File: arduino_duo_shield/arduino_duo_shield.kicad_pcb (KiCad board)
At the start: 2 copper layers, 101.6 x 86.1 mm, 63 parts, among them J1 Spindle_Power, J2 Spindle_Control, J3 Motor_Control, J4 Limit_Switches, J5 Spindle_Relay_Power, J6 Spindle_Signal, J7 Power_In, K1 JQC-3F, P1 CONN_01X01, P10 Digital, P11 PWM, P12 PWM, P13 Communication, P14 CONN_01X01, P15 CONN_01X01, P16 CONN_01X01, P17 CONN_01X01, P2 CONN_01X01, P3 CONN_01X01, P4 CONN_01X01, P5 CONN_01X01, P6 CONN_01X01, P7 Power, P8 Analog, P9 Analog, Q1 2N7000, Q2 IRFZ44N, SW1 SW_Push, U1 4504, U2 4504, U3 PC817, U4 74HC14, U5 PC817, U6 74HC14

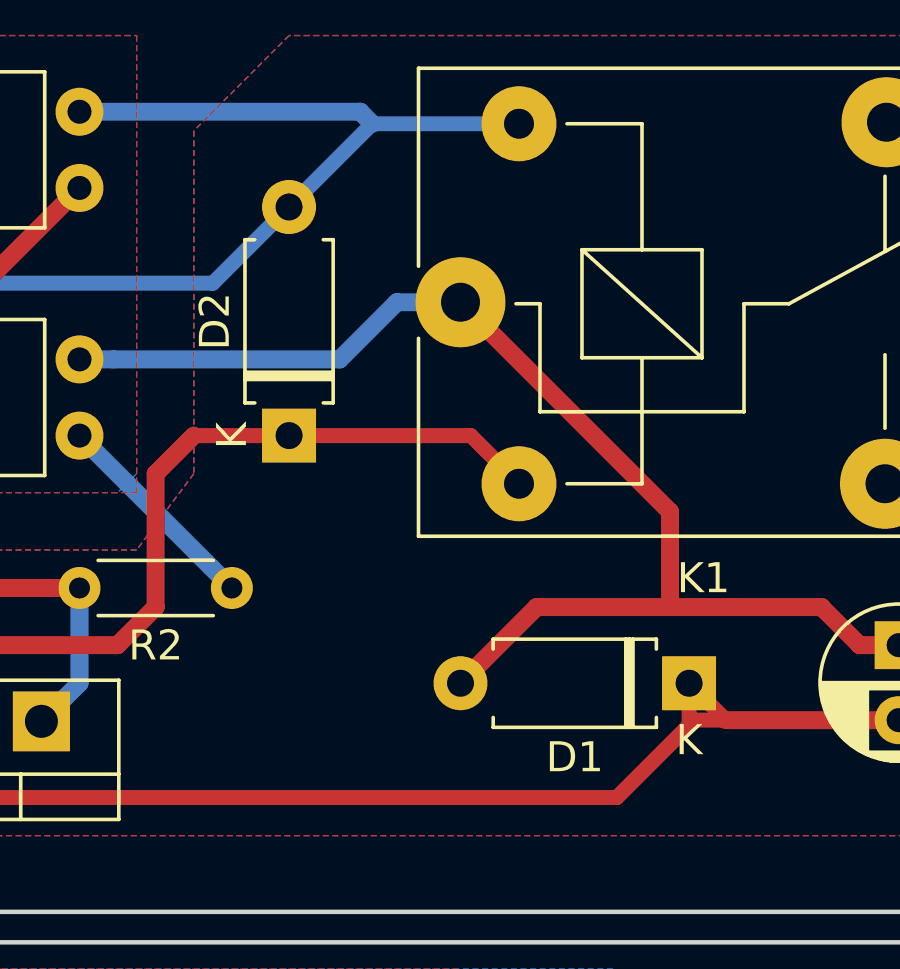
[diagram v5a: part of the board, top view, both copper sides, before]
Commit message: Fix diode symbol in schematic
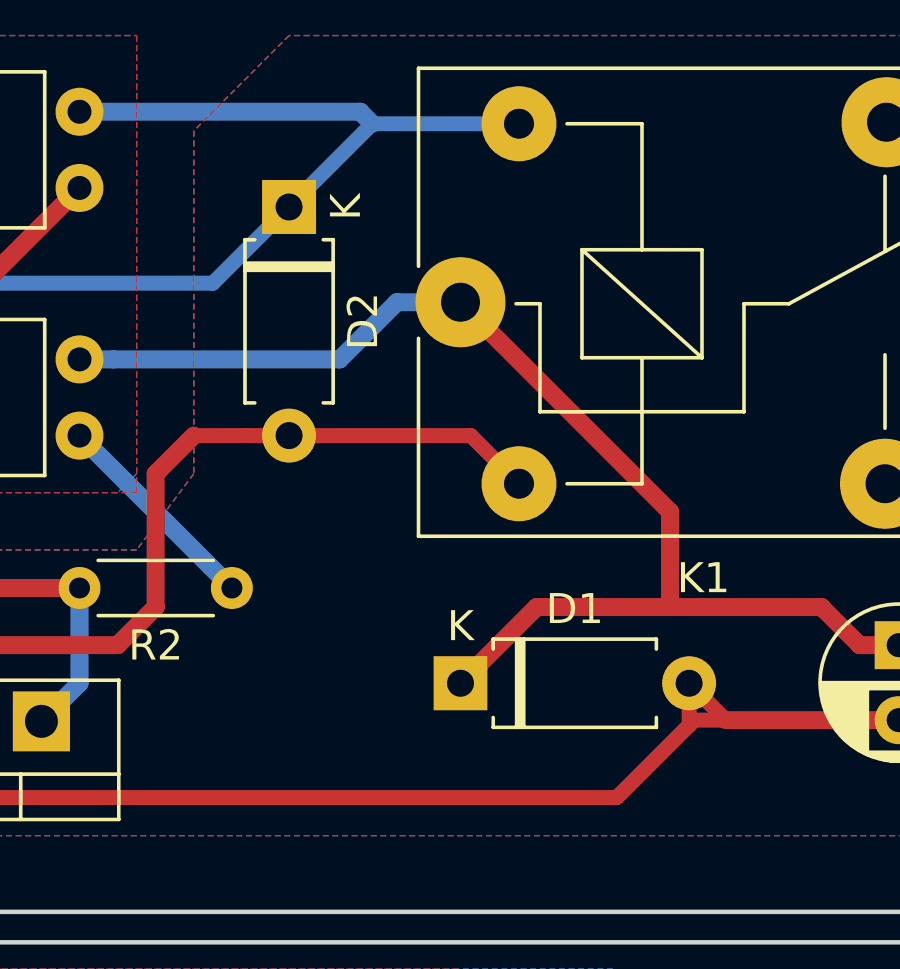
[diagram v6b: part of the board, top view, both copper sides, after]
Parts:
- moved D1 7.62 mm to (147.3, 59.7), turned to 0 degrees
- moved D2 7.62 mm to (141.6, 43.8), turned to 270 degrees
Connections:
- D1 pad 1: Net-(C1-Pad2) -> Net-(C1-Pad1)
- D1 pad 2: Net-(C1-Pad1) -> Net-(C1-Pad2)
- D2 pad 1: Net-(D2-Pad1) -> /Spindle_Power_Control/ext_vcc
- D2 pad 2: /Spindle_Power_Control/ext_vcc -> Net-(D2-Pad2)
- K1 pad 2: Net-(D2-Pad1) -> Net-(D2-Pad2)
- Q1 pad 3: Net-(D2-Pad1) -> Net-(D2-Pad2)
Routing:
- net Net-(D2-Pad2): track 0.00 -> 37.4 mm
- net Net-(D2-Pad1): track 37.4 -> 0.00 mm

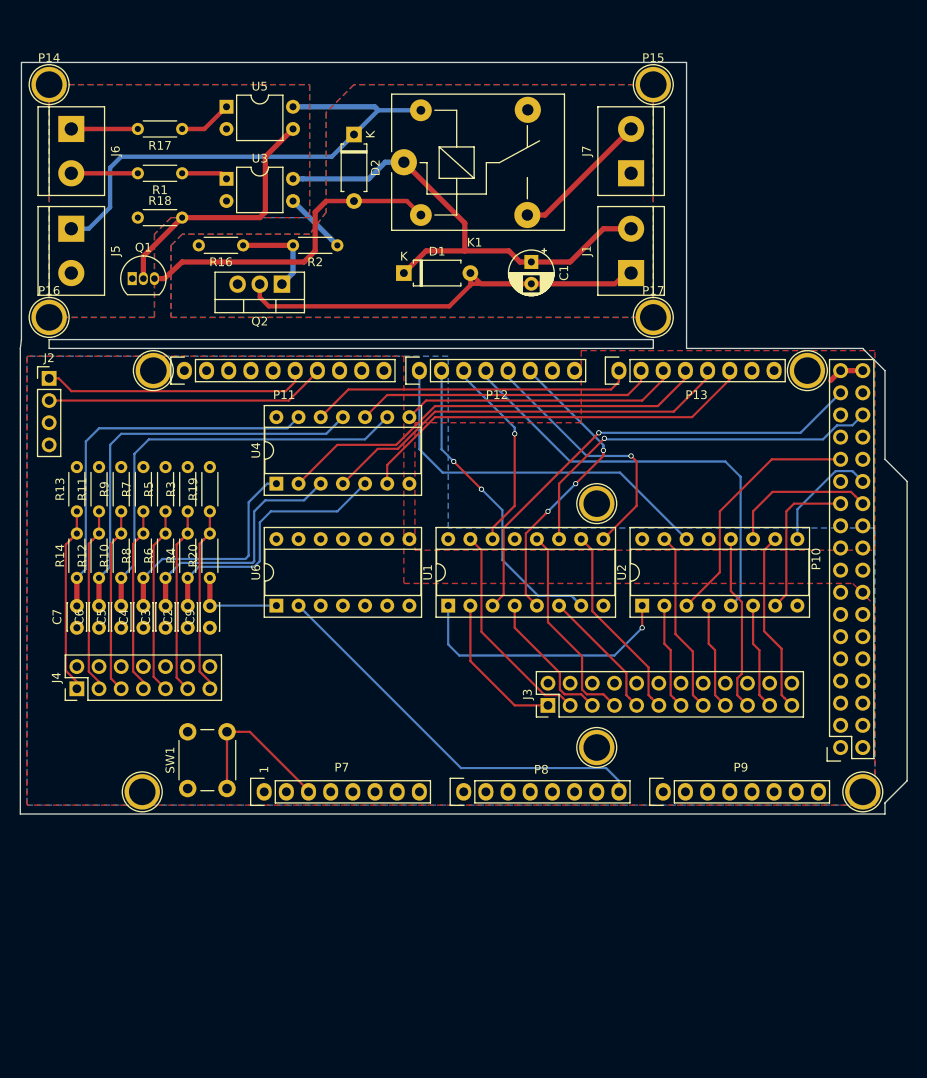
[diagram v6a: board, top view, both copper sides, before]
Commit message: Route all paths
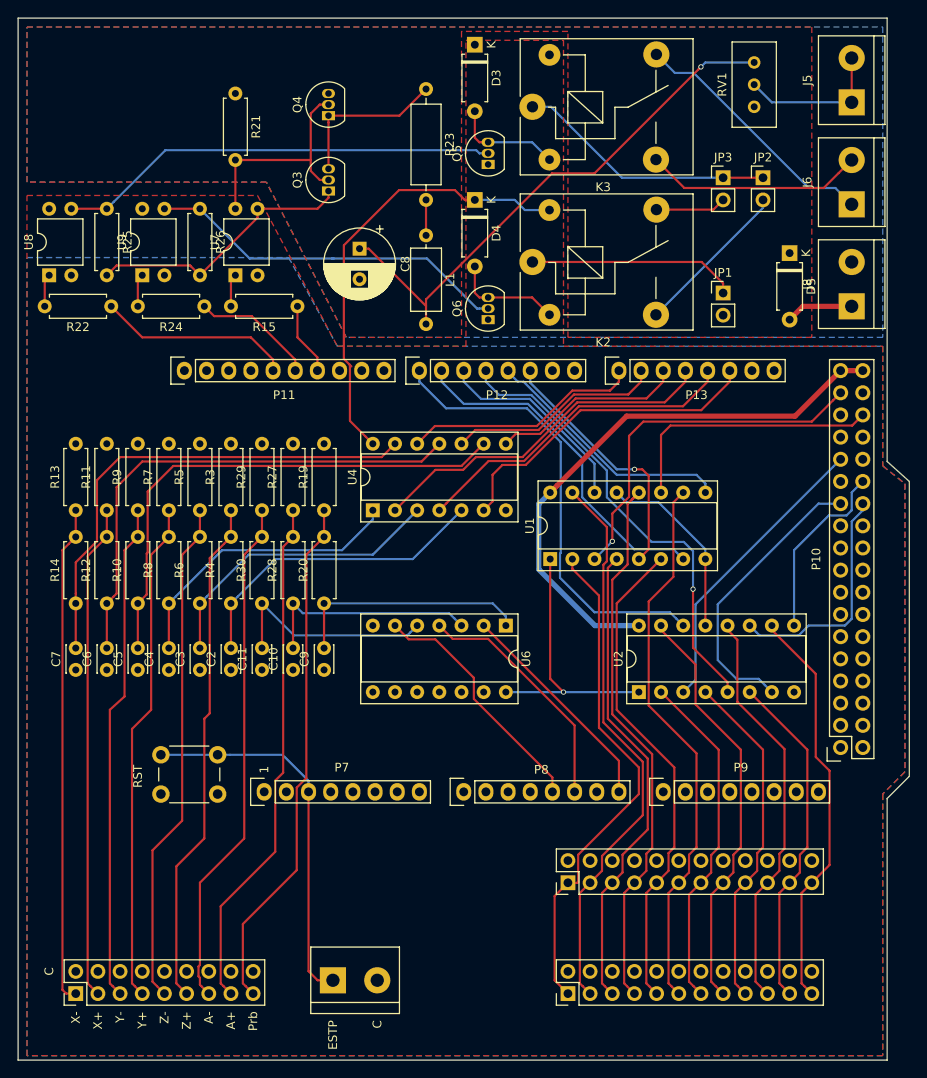
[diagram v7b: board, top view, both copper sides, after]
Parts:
- removed C1: 100u, Capacitor_THT:CP_Radial_D5.0mm_P2.50mm
- removed D1, D2: 1N4007, Diode_THT:D_A-405_P7.62mm_Horizontal
- removed J1: Spindle_Power, TerminalBlock:TerminalBlock_bornier-2_P5.08mm
- removed J7: Power_In, TerminalBlock:TerminalBlock_bornier-2_P5.08mm
- removed K1: JQC-3F, Relay_THT:Relay_SPDT_SANYOU_SRD_Series_Form_C
- removed P1, P14, P15, P16, P17, P2, P3, P4, P5, P6: CONN_01X01, Socket_Arduino_Mega:Arduino_1pin
- removed Q1: 2N7000, Package_TO_SOT_THT:TO-92_Inline
- removed Q2: IRFZ44N, Package_TO_SOT_THT:TO-220-3_Vertical
- removed R1: 220, Resistor_THT:R_Axial_DIN0204_L3.6mm_D1.6mm_P5.08mm_Horizontal
- removed R16: 1K, Resistor_THT:R_Axial_DIN0204_L3.6mm_D1.6mm_P5.08mm_Horizontal
- removed R17: 100, Resistor_THT:R_Axial_DIN0204_L3.6mm_D1.6mm_P5.08mm_Horizontal
- removed R18: 10K, Resistor_THT:R_Axial_DIN0204_L3.6mm_D1.6mm_P5.08mm_Horizontal
- removed R2: 1.3K, Resistor_THT:R_Axial_DIN0204_L3.6mm_D1.6mm_P5.08mm_Horizontal
- removed U3, U5: PC817, Package_DIP:DIP-4_W7.62mm
- added C10: 100p, Capacitor_THT:C_Disc_D3.0mm_W2.0mm_P2.50mm, F.Cu at (134.6, 105.2)
- added C11: 100p, Capacitor_THT:C_Disc_D3.0mm_W2.0mm_P2.50mm, F.Cu at (131.1, 105.2)
- added C8: 100u, Capacitor_THT:CP_Radial_D8.0mm_P3.50mm, F.Cu at (142.2, 56.9)
- added D3: 1N4007, Diode_THT:D_A-405_P7.62mm_Horizontal, F.Cu at (155.4, 33.5)
- added D4: 1N4007, Diode_THT:D_A-405_P7.62mm_Horizontal, F.Cu at (155.4, 51.3)
- added D5: 1N4007, Diode_THT:D_A-405_P7.62mm_Horizontal, F.Cu at (191.5, 57.4)
- added J8: inverter_power, TerminalBlock:TerminalBlock_bornier-2_P5.08mm, F.Cu at (198.6, 63.5)
- added J9: Motor_Control_Mirror, Connector_PinHeader_2.54mm:PinHeader_2x12_P2.54mm_Vertical, F.Cu at (166.1, 142.2)
- added JP1: Jumper_NC_Small, Connector_PinHeader_2.54mm:PinHeader_1x02_P2.54mm_Vertical, F.Cu at (183.9, 62.0)
- added JP2: Jumper_NC_Small, Connector_PinHeader_2.54mm:PinHeader_1x02_P2.54mm_Vertical, F.Cu at (188.5, 48.8)
- added JP3: Jumper_NC_Small, Connector_PinHeader_2.54mm:PinHeader_1x02_P2.54mm_Vertical, F.Cu at (183.9, 48.8)
- added K2: JQC-3F, Relay_THT:Relay_SPDT_SANYOU_SRD_Series_Form_C, F.Cu at (162.1, 58.4)
- added K3: JQC-3F, Relay_THT:Relay_SPDT_SANYOU_SRD_Series_Form_C, F.Cu at (162.1, 40.6)
- added L1: 1m, Inductor_THT:L_Axial_L7.0mm_D3.3mm_P10.16mm_Horizontal_Fastron_MICC, F.Cu at (149.9, 55.4)
- added Q3: 2N7000, Package_TO_SOT_THT:TO-92_Inline, F.Cu at (138.7, 50.3)
- added Q4: BS250, Package_TO_SOT_THT:TO-92_Inline, F.Cu at (138.7, 41.7)
- added Q5: 2N7000, Package_TO_SOT_THT:TO-92_Inline, F.Cu at (157.0, 47.2)
- added Q6: 2N7000, Package_TO_SOT_THT:TO-92_Inline, F.Cu at (157.0, 65.0)
- added R15: 220, Resistor_THT:R_Axial_DIN0207_L6.3mm_D2.5mm_P7.62mm_Horizontal, F.Cu at (135.1, 63.5)
- added R21: 10K, Resistor_THT:R_Axial_DIN0207_L6.3mm_D2.5mm_P7.62mm_Horizontal, F.Cu at (128.0, 39.1)
- added R22: 220, Resistor_THT:R_Axial_DIN0207_L6.3mm_D2.5mm_P7.62mm_Horizontal, F.Cu at (113.8, 63.5)
- added R23: 330, Resistor_THT:R_Axial_DIN0309_L9.0mm_D3.2mm_P12.70mm_Horizontal, F.Cu at (149.9, 38.6)
- added R24: 220, Resistor_THT:R_Axial_DIN0207_L6.3mm_D2.5mm_P7.62mm_Horizontal, F.Cu at (124.5, 63.5)
- added R25: 10K, Resistor_THT:R_Axial_DIN0207_L6.3mm_D2.5mm_P7.62mm_Horizontal, F.Cu at (113.3, 52.3)
- added R26: 10K, Resistor_THT:R_Axial_DIN0207_L6.3mm_D2.5mm_P7.62mm_Horizontal, F.Cu at (124.0, 52.3)
- added R27: 10K, Resistor_THT:R_Axial_DIN0207_L6.3mm_D2.5mm_P7.62mm_Horizontal, F.Cu at (134.6, 86.9)
- added R28: 10K, Resistor_THT:R_Axial_DIN0207_L6.3mm_D2.5mm_P7.62mm_Horizontal, F.Cu at (134.6, 97.5)
- added R29: 10K, Resistor_THT:R_Axial_DIN0207_L6.3mm_D2.5mm_P7.62mm_Horizontal, F.Cu at (131.1, 86.9)
- added R30: 10K, Resistor_THT:R_Axial_DIN0207_L6.3mm_D2.5mm_P7.62mm_Horizontal, F.Cu at (131.1, 97.5)
- added RV1: 100K, Potentiometer_THT:Potentiometer_Bourns_3296W_Vertical, F.Cu at (187.5, 35.6)
- added U7: PC817, Package_DIP:DIP-4_W7.62mm, F.Cu at (128.0, 59.9)
- added U8: PC817, Package_DIP:DIP-4_W7.62mm, F.Cu at (106.7, 59.9)
- added U9: PC817, Package_DIP:DIP-4_W7.62mm, F.Cu at (117.3, 59.9)
- J2: value Spindle_Control -> EStop; footprint Connector_PinHeader_2.54mm:PinHeader_1x04_P2.54mm_Vertical -> TerminalBlock:TerminalBlock_bornier-2_P5.08mm
- J4: footprint Connector_PinHeader_2.54mm:PinHeader_2x07_P2.54mm_Vertical -> Connector_PinHeader_2.54mm:PinHeader_2x09_P2.54mm_Vertical
- J5: value Spindle_Relay_Power -> inverter_freq
- J6: value Spindle_Signal -> inverter_cmd
- R10, R11, R12, R13, R14, R19, R20, R3, R4, R5, R6, R7, R8, R9: footprint Resistor_THT:R_Axial_DIN0204_L3.6mm_D1.6mm_P5.08mm_Horizontal -> Resistor_THT:R_Axial_DIN0207_L6.3mm_D2.5mm_P7.62mm_Horizontal
- moved J5 90.6 mm to (198.6, 40.1), turned to 90 degrees
- moved J6 89.8 mm to (198.6, 51.8), turned to 90 degrees
- moved J2 76.2 mm to (139.2, 140.7)
- moved J4 34.9 mm to (109.7, 142.2)
- moved U6 26.4 mm to (159.0, 100.1), turned to 270 degrees
- moved J3 20.4 mm to (166.1, 129.5)
- moved C9 13.9 mm to (138.2, 105.2)
- moved R20 13.4 mm to (138.2, 97.5)
- moved R19 13.1 mm to (138.2, 86.9)
- moved U1 12.8 mm to (164.1, 92.5)
- moved U4 11.5 mm to (143.8, 86.9)
- moved U2 9.91 mm to (174.2, 107.7)
- moved C2 6.92 mm to (127.5, 105.2)
- moved C3 6.23 mm to (124.0, 105.2)
- moved R4 5.75 mm to (127.5, 97.5)
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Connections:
- J2 pad 1: spenab -> /Reset
- J2 pad 2: sppwm -> GND
- J4 pad 13: /Debounce_x6/SWProbe+ -> /Debounce_x6/SWAmin+
- J5 pad 1: /Spindle_Power_Control/ext_vcc -> /Spindle_VFD_Control/inverter_frequency_10V
- J5 pad 2: /Spindle_Power_Control/ext_gnd -> /Spindle_VFD_Control/inverter_frequency_10V
- J6 pad 1: /Spindle_Power_Control/ext_spenab -> /Spindle_VFD_Control/inverter_fw_switch
- J6 pad 2: /Spindle_Power_Control/ext_sppwm -> /Spindle_VFD_Control/inverter_bw_switch
- P11 pad 5: /13(**) -> spdir
- P8 pad 5: /A4 -> Amn
- P8 pad 6: /A5 -> Amx
- U6 pad 3: (no net) -> Net-(C10-Pad2)
- U6 pad 4: (no net) -> Amx
- U6 pad 5: (no net) -> Net-(C11-Pad2)
- U6 pad 6: (no net) -> Amn
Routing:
- net Net-(C8-Pad1): track 0.00 -> 62.0 mm, vias 0 -> 1
- net +5V: track 4.16 -> 65.1 mm
- net /Debounce_x6/SWAmax+: track 0.00 -> 59.3 mm
- net /Debounce_x6/SWAmin+: track 0.00 -> 58.9 mm
- net /Spindle_Power_Control/ext_vcc: track 58.3 -> 0.00 mm
- net Net-(C1-Pad1): track 55.7 -> 0.00 mm
- net +3V3: track 31.1 -> 82.6 mm
- net Net-(Q5-Pad2): track 0.00 -> 50.7 mm
- net Net-(C1-Pad2): track 49.2 -> 0.00 mm
- net Net-(Q6-Pad2): track 0.00 -> 42.0 mm
- net /Level_Shifter/hi_1_5: track 15.1 -> 56.4 mm
- net /Level_Shifter/hi_1_1: track 17.3 -> 58.2 mm
- net /Level_Shifter/hi_1_6: track 22.7 -> 63.1 mm
- net /Level_Shifter/hi_1_2: track 24.8 -> 64.6 mm
- net /Level_Shifter/hi_1_4: track 23.8 -> 63.5 mm
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- added copper zone on F.Cu, net /Spindle_VFD_Control/I_PWRSAFE
- added copper zone on B.Cu, net /Spindle_VFD_Control/inverter_gnd
- removed copper zone on F.Cu, net +5V
- removed copper zone on B.Cu, net /Spindle_Power_Control/ext_gnd
- removed copper zone on F.Cu, net /Spindle_Power_Control/ext_gnd
- removed copper zone on B.Cu, net MOTOR_GND
- removed copper zone on F.Cu, net MOTOR_GND
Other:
- board size 101.6 x 86.1 mm -> 102.1 x 119.4 mm
- board text added: "A+"
- board text added: "A-"
- board text added: "C"
- board text added: "ESTP"
- board text added: "Prb"
- board text added: "RST"
- board text added: "X+"
- board text added: "X-"
- board text added: "Y+"
- board text added: "Y-"
- board text added: "Z+"
- board text added: "Z-"

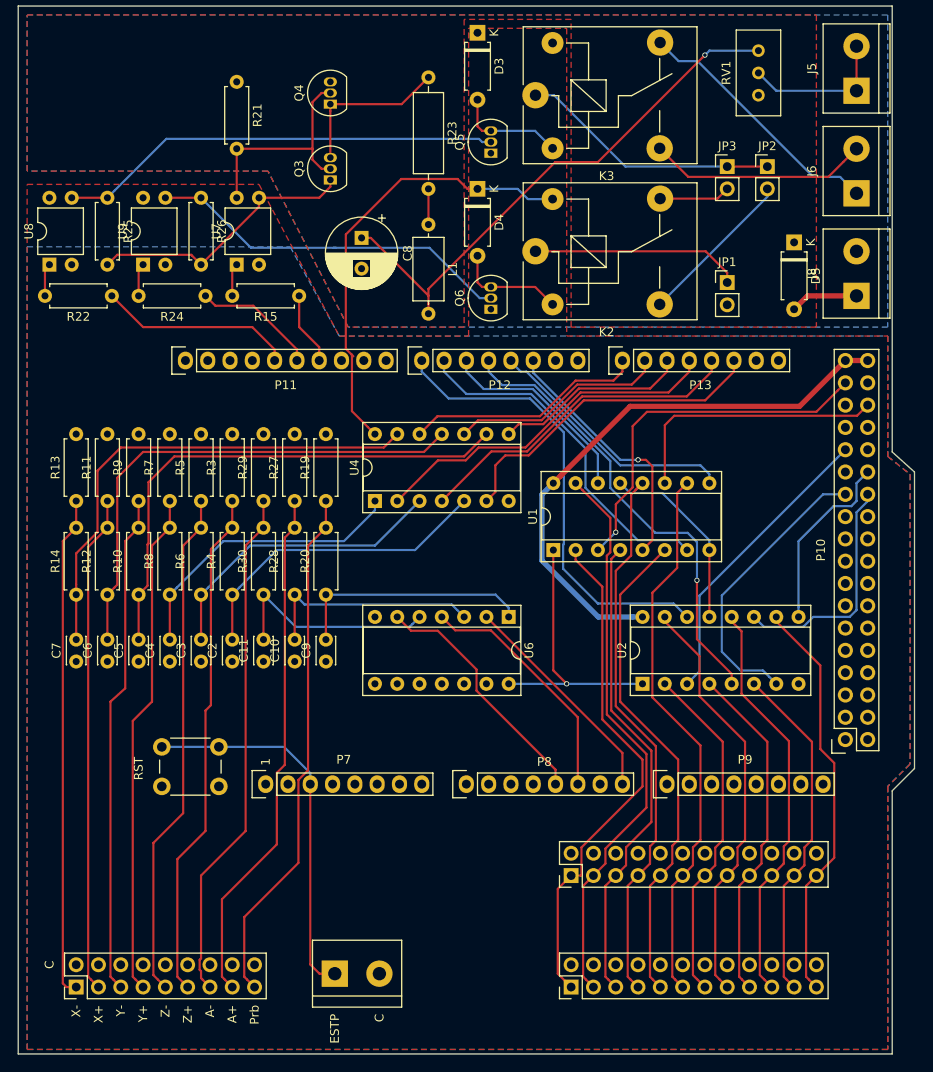
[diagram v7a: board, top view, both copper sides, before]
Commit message: Add silk screen labels and version number
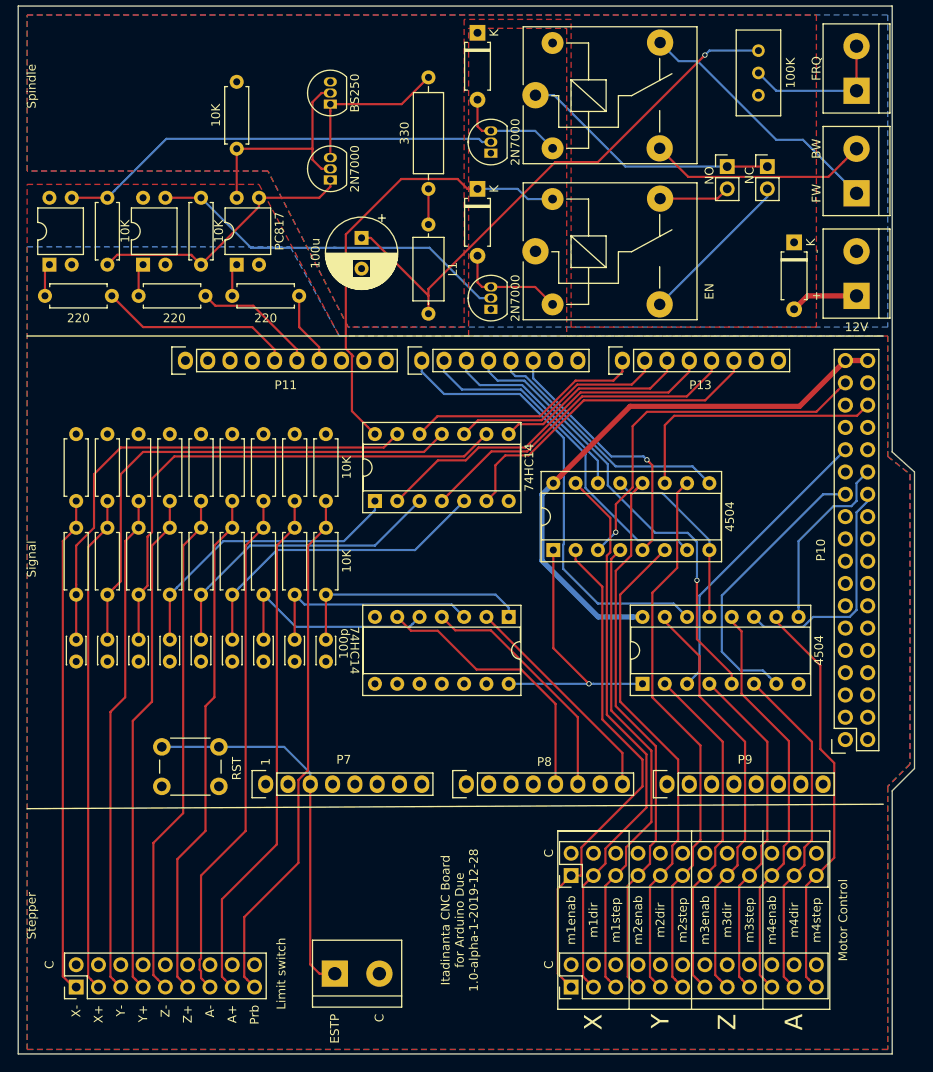
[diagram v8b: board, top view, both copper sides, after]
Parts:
- removed JP1: Jumper_NC_Small, Connector_PinHeader_2.54mm:PinHeader_1x02_P2.54mm_Vertical
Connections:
- K2 pad 1: Net-(JP1-Pad1) -> /Spindle_VFD_Control/inverter_gnd
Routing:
- net Net-(JP1-Pad1): track 24.0 -> 0.00 mm
- net Amn: track 28.3 -> 31.3 mm
- net +3V3: track 82.6 -> 83.7 mm
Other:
- board text added: "+"
- board text added: "-"
- board text added: "12V"
- board text added: "A"
- board text added: "BW"
- board text added: "EN"
- board text added: "FRQ"
- board text added: "FW"
- board text added: "Itadinanta CNC Board for Arduino Due 1.0-alpha-1-2019-12-28"
- board text added: "Limit switch"
- board text added: "Motor Control"
- board text added: "NC"
- board text added: "NO"
- board text added: "Signal"
- board text added: "Spindle"
- board text added: "Stepper"
- board text added: "X"
- board text added: "Y"
- board text added: "Z"
- board text added: "m1dir"
- board text added: "m1enab"
- board text added: "m1step"
- board text added: "m2dir"
- board text added: "m2enab"
- board text added: "m2step"
- board text added: "m3dir"
- board text added: "m3enab"
- board text added: "m3step"
- board text added: "m4dir"
- board text added: "m4enab"
- board text added: "m4step"
